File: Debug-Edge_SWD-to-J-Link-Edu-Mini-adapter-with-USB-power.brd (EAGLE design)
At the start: 21 x 8.9 mm, 8 parts, among them J1 AVX_6-PIN_009159006061916, J3 CORTEX_DEBUG_SMD, J4 10118194-0001LF, U1 MIC5504-3.3YM5-TR

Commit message: Updated README. Added PCB images.
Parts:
- FRAME1: value FRAME-LETTER -> FRAME-LETTERNO_PACKAGE; device SparkFun-Aesthetics:CREATIVE_COMMONS -> SparkFun-Aesthetics:DUMMY
- moved FRAME1 11.4 mm to (0.00, 0.00)
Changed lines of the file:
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@@
 <layers>
 <layer number="1" name="Top" color="4" fill="1" visible="yes" active="yes"/>
-<layer number="16" name="Bottom" color="1" fill="1" visible="yes" active="yes"/>
+<layer number="16" name="Bottom" color="1" fill="1" visible="no" active="yes"/>
 <layer number="17" name="Pads" color="2" fill="1" visible="yes" active="yes"/>
 <layer number="18" name="Vias" color="2" fill="1" visible="yes" active="yes"/>
@@
 <layer number="20" name="Dimension" color="24" fill="1" visible="yes" active="yes"/>
 <layer number="21" name="tPlace" color="7" fill="1" visible="yes" active="yes"/>
-<layer number="22" name="bPlace" color="7" fill="1" visible="yes" active="yes"/>
+<layer number="22" name="bPlace" color="7" fill="1" visible="no" active="yes"/>
 <layer number="23" name="tOrigins" color="15" fill="1" visible="yes" active="yes"/>
-<layer number="24" name="bOrigins" color="15" fill="1" visible="yes" active="yes"/>
+<layer number="24" name="bOrigins" color="15" fill="1" visible="no" active="yes"/>
 <layer number="25" name="tNames" color="7" fill="1" visible="yes" active="yes"/>
-<layer number="26" name="bNames" color="7" fill="1" visible="yes" active="yes"/>
-<layer number="27" name="tValues" color="7" fill="1" visible="yes" active="yes"/>
-<layer number="28" name="bValues" color="7" fill="1" visible="yes" active="yes"/>
+<layer number="26" name="bNames" color="7" fill="1" visible="no" active="yes"/>
+<layer number="27" name="tValues" color="7" fill="1" visible="no" active="yes"/>
+<layer number="28" name="bValues" color="7" fill="1" visible="no" active="yes"/>
 <layer number="29" name="tStop" color="7" fill="3" visible="no" active="yes"/>
 <layer number="30" name="bStop" color="7" fill="6" visible="no" active="yes"/>
@@
 <layer number="38" name="bTest" color="7" fill="1" visible="no" active="yes"/>
 <layer number="39" name="tKeepout" color="4" fill="11" visible="yes" active="yes"/>
-<layer number="40" name="bKeepout" color="1" fill="11" visible="yes" active="yes"/>
+<layer number="40" name="bKeepout" color="1" fill="11" visible="no" active="yes"/>
 <layer number="41" name="tRestrict" color="4" fill="10" visible="yes" active="yes"/>
-<layer number="42" name="bRestrict" color="1" fill="10" visible="yes" active="yes"/>
-<layer number="43" name="vRestrict" color="2" fill="10" visible="yes" active="yes"/>
+<layer number="42" name="bRestrict" color="1" fill="10" visible="no" active="yes"/>
+<layer number="43" name="vRestrict" color="2" fill="10" visible="no" active="yes"/>
 <layer number="44" name="Drills" color="7" fill="1" visible="no" active="yes"/>
 <layer number="45" name="Holes" color="7" fill="1" visible="no" active="yes"/>
 <layer number="46" name="Milling" color="3" fill="1" visible="no" active="yes"/>
 <layer number="47" name="Measures" color="7" fill="1" visible="no" active="yes"/>
-<layer number="48" name="Document" color="7" fill="1" visible="yes" active="yes"/>
-<layer number="49" name="Reference" color="7" fill="1" visible="yes" active="yes"/>
+<layer number="48" name="Document" color="7" fill="1" visible="no" active="yes"/>
+<layer number="49" name="Reference" color="7" fill="1" visible="no" active="yes"/>
 <layer number="50" name="dxf" color="7" fill="1" visible="no" active="no"/>
 <layer number="51" name="tDocu" color="7" fill="1" visible="yes" active="yes"/>
-<layer number="52" name="bDocu" color="7" fill="1" visible="yes" active="yes"/>
+<layer number="52" name="bDocu" color="7" fill="1" visible="no" active="yes"/>
 <layer number="53" name="tGND_GNDA" color="7" fill="9" visible="no" active="no"/>
 <layer number="54" name="bGND_GNDA" color="1" fill="9" visible="no" active="no"/>
@@
 <layer number="115" name="ReferenceISLANDS" color="7" fill="1" visible="no" active="no"/>
 <layer number="116" name="Patch_BOT" color="9" fill="4" visible="no" active="no"/>
-<layer number="117" name="PM_Ref" color="26" fill="1" visible="yes" active="yes"/>
+<layer number="117" name="PM_Ref" color="26" fill="1" visible="no" active="yes"/>
 <layer number="118" name="Rect_Pads" color="7" fill="1" visible="no" active="no"/>
-<layer number="119" name="PF_Ref" color="31" fill="1" visible="yes" active="yes"/>
-<layer number="120" name="WFL_Ref" color="25" fill="1" visible="yes" active="yes"/>
+<layer number="119" name="PF_Ref" color="31" fill="1" visible="no" active="yes"/>
+<layer number="120" name="WFL_Ref" color="25" fill="1" visible="no" active="yes"/>
 <layer number="121" name="_tsilk" color="7" fill="1" visible="no" active="no"/>
 <layer number="122" name="_bsilk" color="7" fill="1" visible="no" active="no"/>
@@
 <layer number="128" name="_bValues" color="7" fill="1" visible="no" active="no"/>
 <layer number="129" name="Mask" color="7" fill="1" visible="no" active="no"/>
-<layer number="130" name="SMDSTROOK" color="7" fill="1" visible="yes" active="yes"/>
+<layer number="130" name="SMDSTROOK" color="7" fill="1" visible="no" active="yes"/>
 <layer number="131" name="tAdjust" color="7" fill="1" visible="no" active="no"/>
 <layer number="132" name="bAdjust" color="7" fill="1" visible="no" active="no"/>
-<layer number="133" name="bottom_silk" color="7" fill="1" visible="yes" active="yes"/>
+<layer number="133" name="bottom_silk" color="7" fill="1" visible="no" active="yes"/>
 <layer number="134" name="silk_top" color="7" fill="1" visible="no" active="no"/>
 <layer number="135" name="silk_bottom" color="7" fill="1" visible="no" active="no"/>
-<layer number="136" name="silktop" color="7" fill="1" visible="yes" active="yes"/>
-<layer number="137" name="silkbottom" color="7" fill="1" visible="yes" active="yes"/>
+<layer number="136" name="silktop" color="7" fill="1" visible="no" active="yes"/>
+<layer number="137" name="silkbottom" color="7" fill="1" visible="no" active="yes"/>
 <layer number="144" name="Drill_legend" color="7" fill="1" visible="no" active="no"/>
-<layer number="145" name="DrillLegend_01-16" color="7" fill="1" visible="yes" active="yes"/>
-<layer number="146" name="DrillLegend_01-20" color="7" fill="1" visible="yes" active="yes"/>
+<layer number="145" name="DrillLegend_01-16" color="7" fill="1" visible="no" active="yes"/>
+<layer number="146" name="DrillLegend_01-20" color="7" fill="1" visible="no" active="yes"/>
 <layer number="150" name="Notes" color="7" fill="1" visible="no" active="no"/>
 <layer number="151" name="HeatSink" color="7" fill="1" visible="no" active="no"/>
@@
 <layer number="154" name="FabDoc2" color="7" fill="1" visible="no" active="no"/>
 <layer number="155" name="FabDoc3" color="7" fill="1" visible="no" active="no"/>
-<layer number="166" name="AntennaArea" color="7" fill="1" visible="yes" active="yes"/>
-<layer number="168" name="4mmHeightArea" color="7" fill="1" visible="yes" active="yes"/>
+<layer number="166" name="AntennaArea" color="7" fill="1" visible="no" active="yes"/>
+<layer number="168" name="4mmHeightArea" color="7" fill="1" visible="no" active="yes"/>
 <layer number="199" name="Contour" color="7" fill="1" visible="no" active="no"/>
 <layer number="200" name="200bmp" color="1" fill="10" visible="no" active="no"/>
@@
 </autorouter>
 <elements>
-<element name="FRAME1" library="SparkFun-Aesthetics" package="CREATIVE_COMMONS" value="FRAME-LETTER" x="0.635" y="11.43" smashed="yes">
-<attribute name="DESIGNER" value="" x="80.645" y="-3.81" size="1.778" layer="27" display="off"/>
-<attribute name="REV" value="" x="80.645" y="-3.81" size="1.778" layer="27" display="off"/>
-</element>
 <element name="C1" library="adafruit" package="C0805" value="1uF" x="6.35" y="2.54" smashed="yes" rot="MR0">
 <attribute name="NAME" x="6.096" y="1.524" size="0.8128" layer="26" ratio="6" rot="MR180"/>
@@
 <attribute name="VENDOR" value="Microchip" x="10.795" y="4.445" size="1.778" layer="28" rot="MR90" display="off"/>
 </element>
+<element name="FRAME1" library="SparkFun-Aesthetics" package="DUMMY" value="FRAME-LETTERNO_PACKAGE" x="0" y="0" smashed="yes">
+<attribute name="DESIGNER" value="Nathan Jones" x="0" y="0" size="1.778" layer="27" display="off"/>
+<attribute name="VERSION" value="v01" x="0" y="0" size="1.778" layer="27" display="off"/>
+</element>
 </elements>

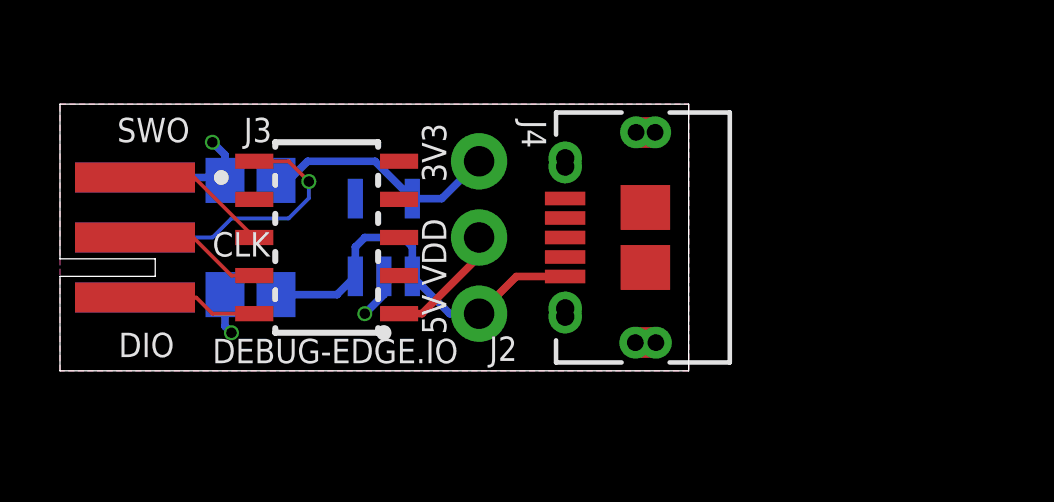
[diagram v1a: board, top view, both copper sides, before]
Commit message: Updated AVX library. Changed to PTH components.
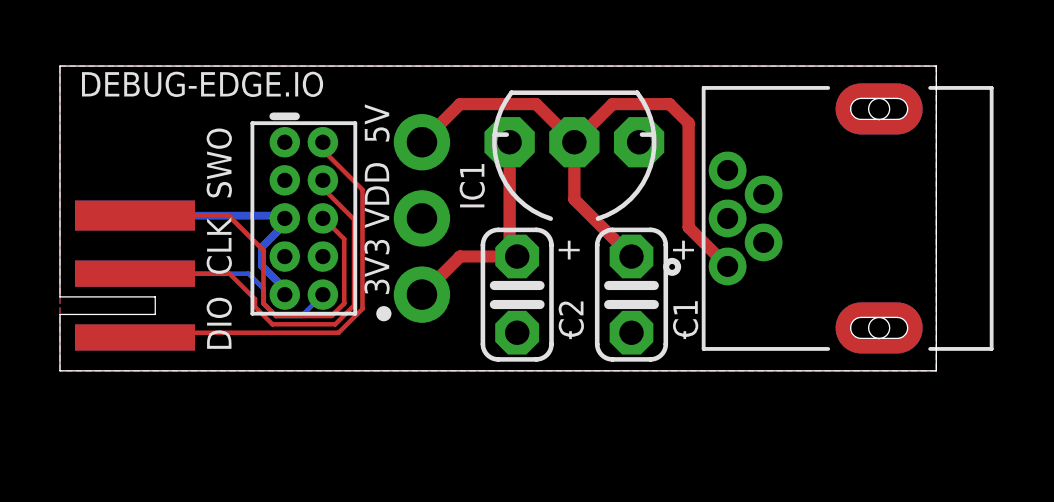
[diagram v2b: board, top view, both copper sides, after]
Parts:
- removed U1: MIC5504-3.3YM5-TR, MIC5504-3.3YM5-TR:SOT-23-5_MC_MCH
- added IC1: (no value), adafruit:TO92-INLINE
- C1, C2: value 1uF -> (none); device adafruit:C0805 -> adafruit:C025-024X044
- J3: value CORTEX_DEBUG_SMD -> CORTEX_DEBUG_PTH; device SparkFun-Connectors:SAMTECH_FTSH-105-01 -> SparkFun-Connectors:2X5-PTH-1.27MM
- J4: value 10118194-0001LF -> 2172034-1; device USB-micro-B_Amphenol_10118194-0001LF:CONN_10118194-0001LF_AMP -> USB-mini-B_TE_2172034-1:TE_2172034-1
- moved C1 12.7 mm to (19.1, 2.54), flipped to the top, turned to 270 degrees
- moved C2 9.67 mm to (15.2, 2.54), flipped to the top, turned to 270 degrees
- moved J4 7.90 mm to (27.3, 5.08), turned to 0 degrees
- moved J2 4.84 mm to (12.1, 2.54), turned to 90 degrees
- moved J1 1.27 mm to (0.00, 3.17), flipped to the bottom, turned to 90 degrees
- moved FRAME1 1.27 mm to (0.00, -1.27)
- moved J3 0.99 mm to (8.13, 5.08), turned to 270 degrees
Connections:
- net 3V3: now also IC1.3; no longer U1.5
- net 5V: now also IC1.2; no longer U1.1, U1.3
- net GND: now also IC1.1, J1.3, J3.5, J3.9, J4.SH1, J4.SH2; no longer J1.4, J4.10, J4.11, J4.4, J4.S_1, J4.S_1_H1, J4.S_1_H2, J4.S_2, J4.S_2_H1, J4.S_2_H2, J4.S_3, J4.S_3_H1, J4.S_3_H2, J4.S_4, J4.S_4_H1, J4.S_4_H2, U1.2
- net NRST: now also J1.2; no longer J1.5
- net SWCLK: now also J1.5; no longer J1.2
- net SWDIO: now also J1.4; no longer J1.3
- net SWO: now also J1.6; no longer J1.1
- net VTREF: now also J1.1; no longer J1.6
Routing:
- net SWDIO: track 4.20 -> 14.1 mm
- net SWCLK: track 4.50 -> 13.0 mm
- net SWO: track 4.81 -> 12.7 mm
- net 5V: track 13.1 -> 20.6 mm
- net VTREF: track 4.09 -> 0.00 mm
- net NRST: track 8.99 -> 7.43 mm, vias 1 -> 0
- net GND: track 7.35 -> 8.20 mm, vias 3 -> 0
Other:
- board size 21 x 8.9 mm -> 29.2 x 10.2 mm
- board text added: "- +"
